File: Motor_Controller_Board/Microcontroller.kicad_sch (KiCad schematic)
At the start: 20 parts, among them J301 Conn_01x04, J303 USB_B_Micro, SW301 SW_Push, U301 AMS1117, U303 ESP32-C6-MINI-1

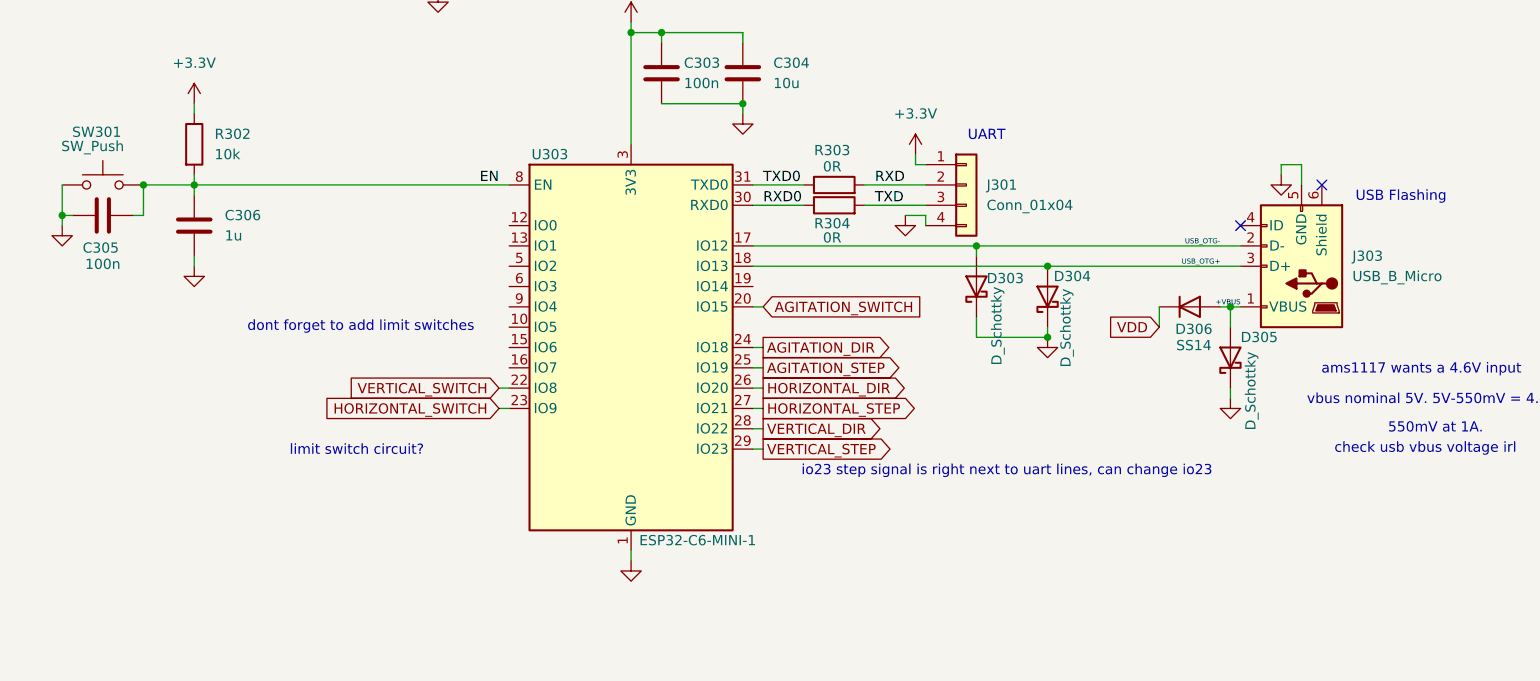
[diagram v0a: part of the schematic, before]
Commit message: picking footprints. still need buck regulator footprints
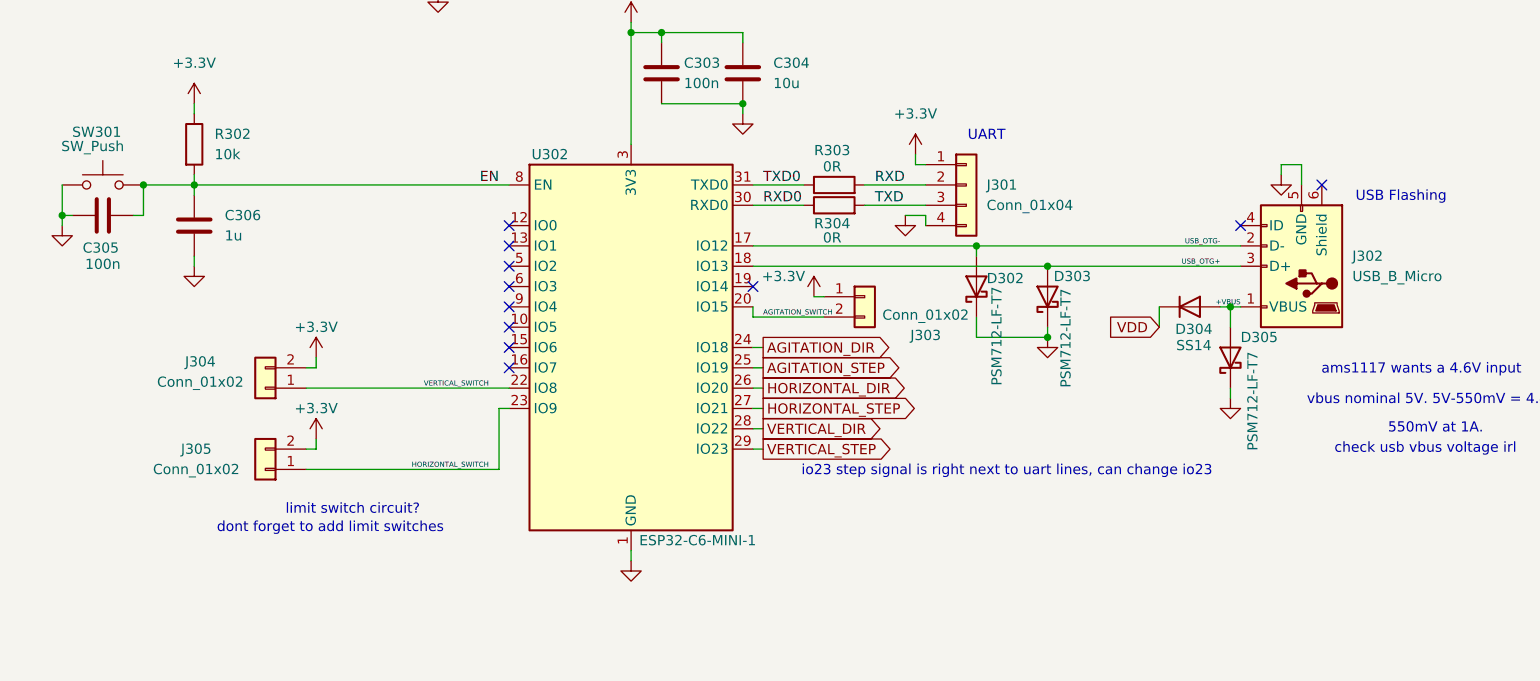
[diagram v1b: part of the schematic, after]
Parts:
- added J303, J304, J305: Conn_01x02, Connector_PinHeader_2.54mm:PinHeader_1x02_P2.54mm_Vertical, symbol Connector_Generic:Conn_01x02
- C301, C302, C303, C304, C305, C306: footprint (none) -> Capacitor_SMD:C_0603_1608Metric
- D301: footprint (none) -> LED_SMD:LED_0603_1608Metric
- D302: renamed from D303; value D_Schottky -> PSM712-LF-T7; footprint (none) -> Package_TO_SOT_SMD:SOT-23
- D303: renamed from D304; value D_Schottky -> PSM712-LF-T7; footprint (none) -> Package_TO_SOT_SMD:SOT-23
- D304: renamed from D306; footprint (none) -> Diode_SMD:D_SMA
- D305: value D_Schottky -> PSM712-LF-T7; footprint (none) -> Package_TO_SOT_SMD:SOT-23
- J301: footprint (none) -> Connector_PinHeader_2.54mm:PinHeader_1x04_P2.54mm_Vertical
- J302: renamed from J303; footprint (none) -> Connector_USB:USB_Micro-B_Molex-105017-0001
- R301, R302, R303, R304: footprint (none) -> Resistor_SMD:R_0603_1608Metric
- SW301: footprint (none) -> Button_Switch_SMD:SW_Push_1P1T_XKB_TS-1187A
- renumbered U303 to U302
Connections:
- net +3.3V: now also J303.1 (Pin_1), J304.2 (Pin_2), J305.2 (Pin_2)
- net AGITATION_SWITCH: now also J303.2 (Pin_2)
- net HORIZONTAL_SWITCH: now also J305.1 (Pin_1)
- net VERTICAL_SWITCH: now also J304.1 (Pin_1)
- no-connect marks 2 -> 11

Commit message: schematic and footprints have been selected. ready to start layout, but always open to changes in schematic
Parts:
- added C307: 100n, Capacitor_SMD:C_0402_1005Metric, symbol Device:C
- added R305: 10k, Resistor_SMD:R_0603_1608Metric, symbol Device:R
- added SW302: SW_Push, Button_Switch_SMD:SW_Push_1P1T_XKB_TS-1187A, symbol Switch:SW_Push
- C301, C302: JCSC Part Number (none) -> C45783; MPN (none) -> CL21A226MAQNNNE; Manufacturer (none) -> Samsung Electro-Mechanics
- C303, C305: footprint Capacitor_SMD:C_0603_1608Metric -> Capacitor_SMD:C_0402_1005Metric; JCSC Part Number (none) -> C1525; MPN (none) -> CL05B104KO5NNNC; Manufacturer (none) -> Samsung Electro-Mechanics
- C304: value 10u -> 22u; JCSC Part Number (none) -> C45783; MPN (none) -> CL21A226MAQNNNE; Manufacturer (none) -> Samsung Electro-Mechanics
- C306: footprint Capacitor_SMD:C_0603_1608Metric -> Capacitor_SMD:C_0402_1005Metric; JCSC Part Number (none) -> C52923; MPN (none) -> CL05A105KA5NQNC; Manufacturer (none) -> Samsung Electro-Mechanics
- D301: value GREEN -> RED; JCSC Part Number (none) -> C2286; MPN (none) -> KT-0603R; Manurfacturer (none) -> Hubei KENTO Elec
- D302, D303, D305: JCSC Part Number (none) -> C32677; MPN (none) -> PSM712-LF-T7; Manufacturer (none) -> ProTek Devices
- D304: JCSC Part Number (none) -> C2480; MPN (none) -> SS14; Manufacturer (none) -> MDD(Microdiode Semiconductor)
- J302: JCSC Part Number (none) -> C404969; MPN (none) -> MicroXNJ; Manufacturer (none) -> SHOU HAN
- R301: JCSC Part Number (none) -> C23186; MPN (none) -> 0603WAF5101T5E; Manufacturer (none) -> UNI-ROYAL(Uniroyal Elec)
- R302: JCSC Part Number (none) -> C25804; MPN (none) -> 0603WAF1002T5E; Manufacturer (none) -> UNI-ROYAL(Uniroyal Elec)
- R303, R304: JCSC Part Number (none) -> C21189; MPN (none) -> 0603WAF0000T5E; Manufacturer (none) -> UNI-ROYAL(Uniroyal Elec)
- SW301: JCSC Part Number (none) -> C318884; MPN (none) -> TS-1187A-B-A-B; Manufacturer (none) -> XKB Connection
- U301: JCSC Part Number (none) -> C6186; MPN (none) -> AMS1117-3.3; Manufacturer (none) -> Advanced Monolithic Systems
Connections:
- net +3.3V: now also C303.2, R305.1; no longer C303.1
- net GND: now also C303.1, C307.1, SW302.1; no longer C303.2
- net HORIZONTAL_SWITCH: now also U302.16 (IO7); no longer U302.23 (IO9)
- net VERTICAL_SWITCH: now also U302.15 (IO6); no longer U302.22 (IO8)
- net USB_OTG+ renamed USB_D+
- net USB_OTG- renamed USB_D-
- new net BOOT: C307.2, SW302.2, U302.23 (IO9)
- new net IO8: R305.2, U302.22 (IO8)
- no-connect marks 11 -> 9
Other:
- moved on the sheet: D301, J304, J305, R301, U301

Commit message: changed jcsc to lcsc
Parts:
- C301, C302, C304: JCSC Part Number C45783 -> (none); LCSC Part Number (none) -> C45783
- C303, C305, C307: JCSC Part Number C1525 -> (none); LCSC Part Number (none) -> C1525
- C306: JCSC Part Number C52923 -> (none); LCSC Part Number (none) -> C52923
- D301: JCSC Part Number C2286 -> (none); LCSC Part Number (none) -> C2286; Manufacturer (none) -> Hubei KENTO Elec; Manurfacturer Hubei KENTO Elec -> (none)
- D302, D303, D305: JCSC Part Number C32677 -> (none); LCSC Part Number (none) -> C32677
- D304: JCSC Part Number C2480 -> (none); LCSC Part Number (none) -> C2480
- J301, J303, J304, J305: now left out of the parts list
- J302: JCSC Part Number C404969 -> (none); LCSC Part Number (none) -> C404969
- R301: JCSC Part Number C23186 -> (none); LCSC Part Number (none) -> C23186
- R302, R305: JCSC Part Number C25804 -> (none); LCSC Part Number (none) -> C25804
- R303, R304: JCSC Part Number C21189 -> (none); LCSC Part Number (none) -> C21189
- SW301, SW302: JCSC Part Number C318884 -> (none); LCSC Part Number (none) -> C318884
- U301: JCSC Part Number C6186 -> (none); LCSC Part Number (none) -> C6186
- U302: LCSC Part Number (none) -> C20627095; MPN (none) -> ESP32-C6-MINI-1U-H4; Manufacturer (none) -> Espressif Systems
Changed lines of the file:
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@@
 			)
 		)
-		(property "JCSC Part Number" "C21189"
-			(at 167.64 88.9 90)
+		(property "LCSC Part Number" "C21189"
+			(at 167.64 88.9 0)
 			(effects
 				(font
@@
 			)
 		)
-		(property "JCSC Part Number" "C52923"
+		(property "LCSC Part Number" "C52923"
 			(at 87.63 93.98 0)
 			(effects
@@
 			)
 		)
-		(property "JCSC Part Number" "C32677"
-			(at 194.31 102.87 90)
+		(property "LCSC Part Number" "C32677"
+			(at 194.31 102.87 0)
 			(effects
 				(font
@@
 			)
 		)
-		(property "JCSC Part Number" "C21189"
-			(at 167.64 91.44 90)
+		(property "LCSC Part Number" "C21189"
+			(at 167.64 91.44 0)
 			(effects
 				(font
@@
 			)
 		)
-		(property "JCSC Part Number" "C1525"
+		(property "LCSC Part Number" "C1525"
 			(at 146.05 74.93 90)
 			(effects
@@
 			)
 		)
-		(property "JCSC Part Number" "C45783"
+		(property "LCSC Part Number" "C45783"
 			(at 133.35 74.93 0)
 			(effects
@@
 			)
 		)
-		(property "Manurfacturer" "Hubei KENTO Elec"
+		(property "Manufacturer" "Hubei KENTO Elec"
 			(at 101.6 73.66 90)
 			(effects
@@
 			)
 		)
-		(property "JCSC Part Number" "C2286"
+		(property "LCSC Part Number" "C2286"
 			(at 101.6 73.66 90)
 			(effects
@@
 			)
 		)
-		(property "JCSC Part Number" "C318884"
+		(property "LCSC Part Number" "C318884"
 			(at 118.11 121.92 0)
 			(effects
@@
 			)
 		)
-		(property "JCSC Part Number" "C25804"
+		(property "LCSC Part Number" "C25804"
 			(at 87.63 83.82 0)
 			(effects
@@
 		(unit 1)
 		(exclude_from_sim no)
-		(in_bom yes)
+		(in_bom no)
 		(on_board yes)
 		(dnp no)
@@
 			)
 		)
-		(property "JCSC Part Number" "C25804"
+		(property "LCSC Part Number" "C25804"
 			(at 106.68 114.3 0)
 			(effects
@@
 			)
 		)
-		(property "JCSC Part Number" "C1525"
-			(at 118.11 125.73 90)
+		(property "LCSC Part Number" "C1525"
+			(at 118.11 125.73 0)
 			(effects
 				(font
@@
 			)
 		)
-		(property "JCSC Part Number" "C404969"
+		(property "LCSC Part Number" "C404969"
 			(at 226.06 99.06 0)
 			(effects
@@
 			)
 		)
-		(property "JCSC Part Number" "C23186"
+		(property "LCSC Part Number" "C23186"
 			(at 107.95 68.58 90)
 			(effects
@@
 			)
 		)
+		(property "Manufacturer" "Espressif Systems"
+			(at 142.24 109.22 0)
+			(effects
+				(font
+					(size 1.27 1.27)
+				)
+				(hide yes)
+			)
+		)
+		(property "MPN" "ESP32-C6-MINI-1U-H4"
+			(at 142.24 109.22 0)
+			(effects
+				(font
+					(size 1.27 1.27)
+				)
+				(hide yes)
+			)
+		)
+		(property "LCSC Part Number" "C20627095"
+			(at 142.24 109.22 0)
+			(effects
+				(font
+					(size 1.27 1.27)
+				)
+				(hide yes)
+			)
+		)
 		(pin "17"
 		)
@@
 			)
 		)
-		(property "JCSC Part Number" "C45783"
+		(property "LCSC Part Number" "C45783"
 			(at 156.21 74.93 0)
 			(effects
@@
 			)
 		)
-		(property "JCSC Part Number" "C32677"
-			(at 185.42 101.6 90)
+		(property "LCSC Part Number" "C32677"
+			(at 185.42 101.6 0)
 			(effects
 				(font
@@
 			)
 		)
-		(property "JCSC Part Number" "C32677"
-			(at 217.17 110.49 90)
+		(property "LCSC Part Number" "C32677"
+			(at 217.17 110.49 0)
 			(effects
 				(font
@@
 		(unit 1)
 		(exclude_from_sim no)
-		(in_bom yes)
+		(in_bom no)
 		(on_board yes)
 		(dnp no)
@@
 			)
 		)
-		(property "JCSC Part Number" "C2480"
+		(property "LCSC Part Number" "C2480"
 			(at 212.09 104.14 0)
 			(effects
@@
 		(unit 1)
 		(exclude_from_sim no)
-		(in_bom yes)
+		(in_bom no)
 		(on_board yes)
 		(dnp no)
@@
 			)
 		)
-		(property "JCSC Part Number" "C45783"
+		(property "LCSC Part Number" "C45783"
 			(at 114.3 74.93 0)
 			(effects
@@
 			)
 		)
-		(property "JCSC Part Number" "C1525"
-			(at 76.2 92.71 90)
+		(property "LCSC Part Number" "C1525"
+			(at 76.2 92.71 0)
 			(effects
 				(font
@@
 			)
 		)
-		(property "JCSC Part Number" "C6186"
+		(property "LCSC Part Number" "C6186"
 			(at 124.46 68.58 0)
 			(effects
@@
 		(unit 1)
 		(exclude_from_sim no)
-		(in_bom yes)
+		(in_bom no)
 		(on_board yes)
 		(dnp no)
@@
 			)
 		)
-		(property "JCSC Part Number" "C318884"
+		(property "LCSC Part Number" "C318884"
 			(at 76.2 88.9 0)
 			(effects
